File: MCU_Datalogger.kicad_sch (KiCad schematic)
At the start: 25 parts, among them U1 24LC1025, U2 DS1337S_, U3 24LC1025, U4 ATMEGA328P-AU, Y1 32.768 KHz, Y2 16 MHz

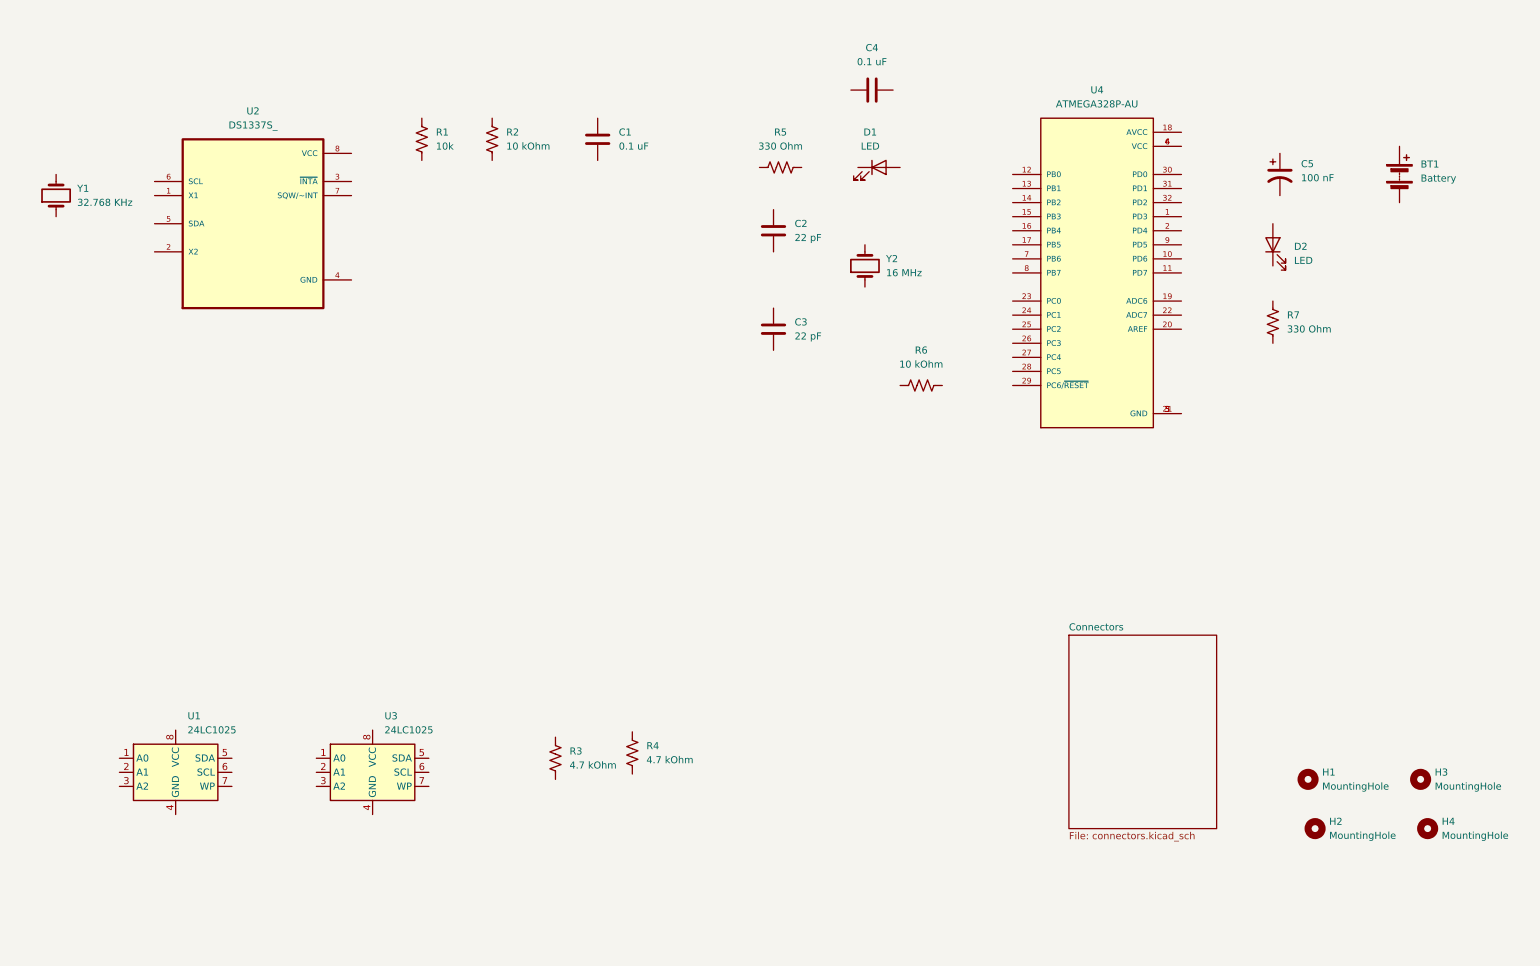
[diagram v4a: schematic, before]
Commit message: Wiring and adding netlabels to the schematic diagram for the main schematic page
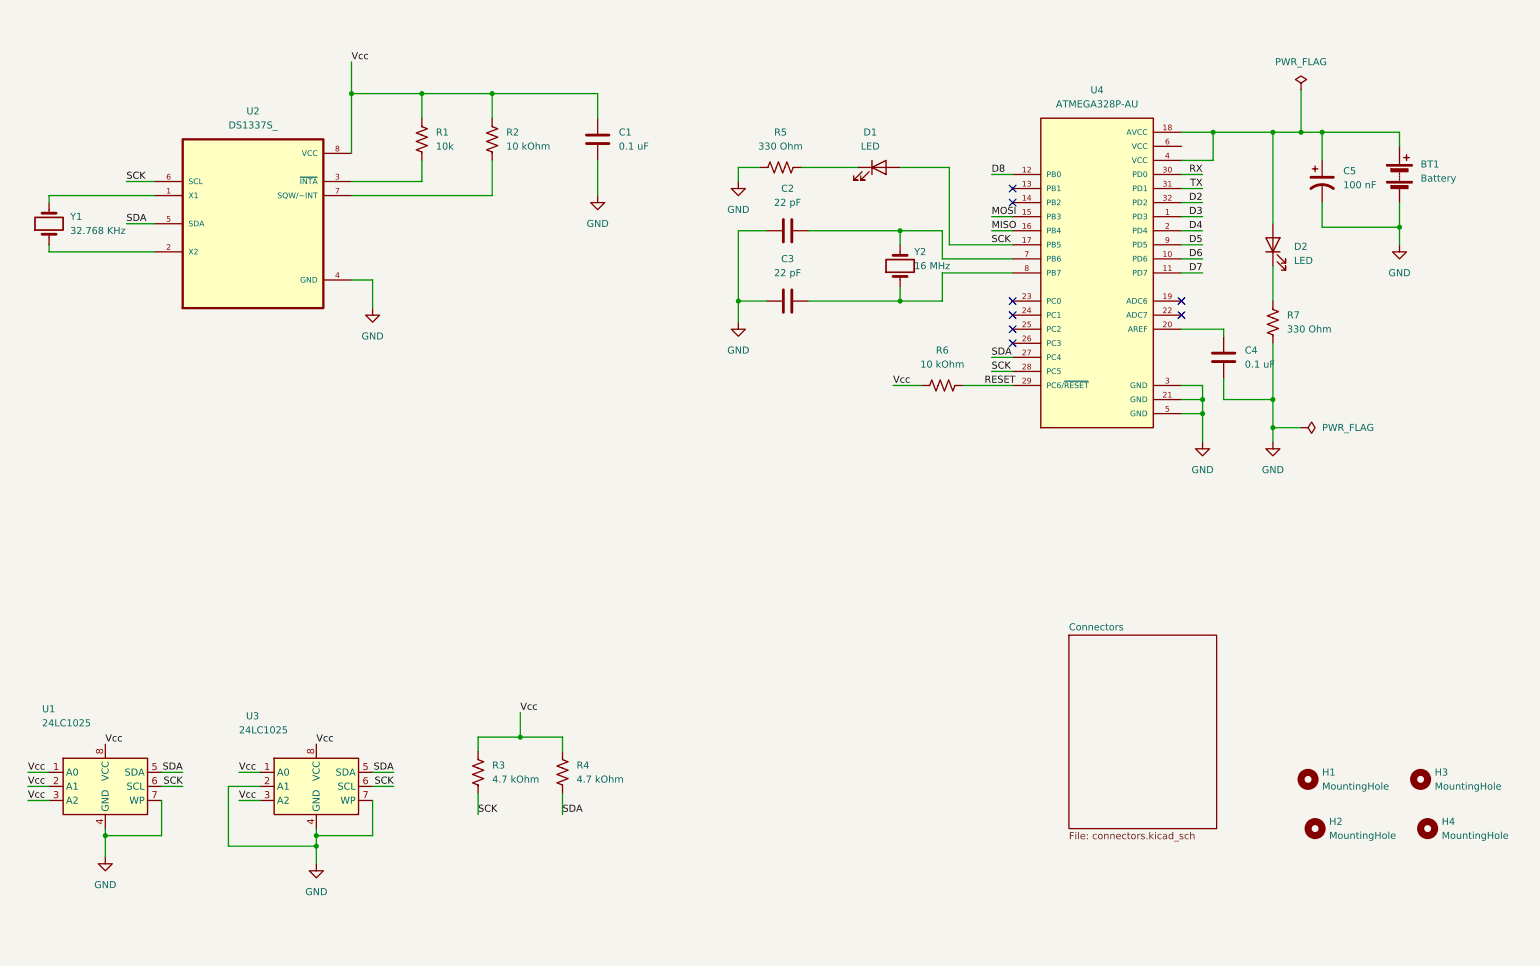
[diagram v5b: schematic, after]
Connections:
- net at U2.1 (X1): now also Y1.2
- net at U2.2 (X2): now also Y1.1
- net at U2.3 (~{INTA}): now also R1.2
- net GND: now reaches U2.4 (GND)
- net GND: now also BT1.2 (-), C1.2, C2.1, C3.1, C4.1, C5.2, R5.1, R7.2, U1.4 (GND), U1.7 (WP), U3.2 (A1), U3.4 (GND), U3.7 (WP), U4.21 (GND), U4.3 (GND), U4.5 (GND)
- net SDA: now reaches U2.5 (SDA)
- net SDA: now also R4.2, U1.5 (SDA), U3.5 (SDA), U4.27 (PC4)
- net SCK: now reaches U2.6 (SCL)
- net SCK: now also D1.2 (A), R3.2, U1.6 (SCL), U3.6 (SCL), U4.17 (PB5), U4.28 (PC5)
- net at U2.7 (SQW/~INT): now also R2.2
- net Vcc: now reaches U2.8 (VCC)
- net Vcc: now also C1.1, R1.1, R2.1, R3.1, R4.1, R6.1, U1.1 (A0), U1.2 (A1), U1.3 (A2), U1.8 (VCC), U3.1 (A0), U3.3 (A2), U3.8 (VCC)
- net at C2.2: now also U4.7 (PB6), Y2.2
- net at BT1.1 (+): now also C5.1, D2.2 (A), U4.18 (AVCC), U4.4 (VCC)
- net RESET: now reaches R6.2
- net RESET: now also U4.29 (PC6/~{RESET})
- net at D2.1 (K): now also R7.1
- net D3: now reaches U4.1 (PD3)
- net D6: now reaches U4.10 (PD6)
- net D7: now reaches U4.11 (PD7)
- net D8: now reaches U4.12 (PB0)
- net MOSI: now reaches U4.15 (PB3)
- net MISO: now reaches U4.16 (PB4)
- net D4: now reaches U4.2 (PD4)
- net at U4.20 (AREF): now also C4.2
- net RX: now reaches U4.30 (PD0)
- net TX: now reaches U4.31 (PD1)
- net D2: now reaches U4.32 (PD2)
- net at U4.6 (VCC): no longer U4.4 (VCC)
- net at U4.8 (PB7): now also C3.2, Y2.1
- net D5: now reaches U4.9 (PD5)
- net at D1.1 (K): now also R5.2
- no-connect marks 0 -> 8
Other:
- moved on the sheet: C2, C3, C4, C5, R3, R6, U1, U3, Y1, Y2

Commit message: Completed schematic wiring and passed ERC
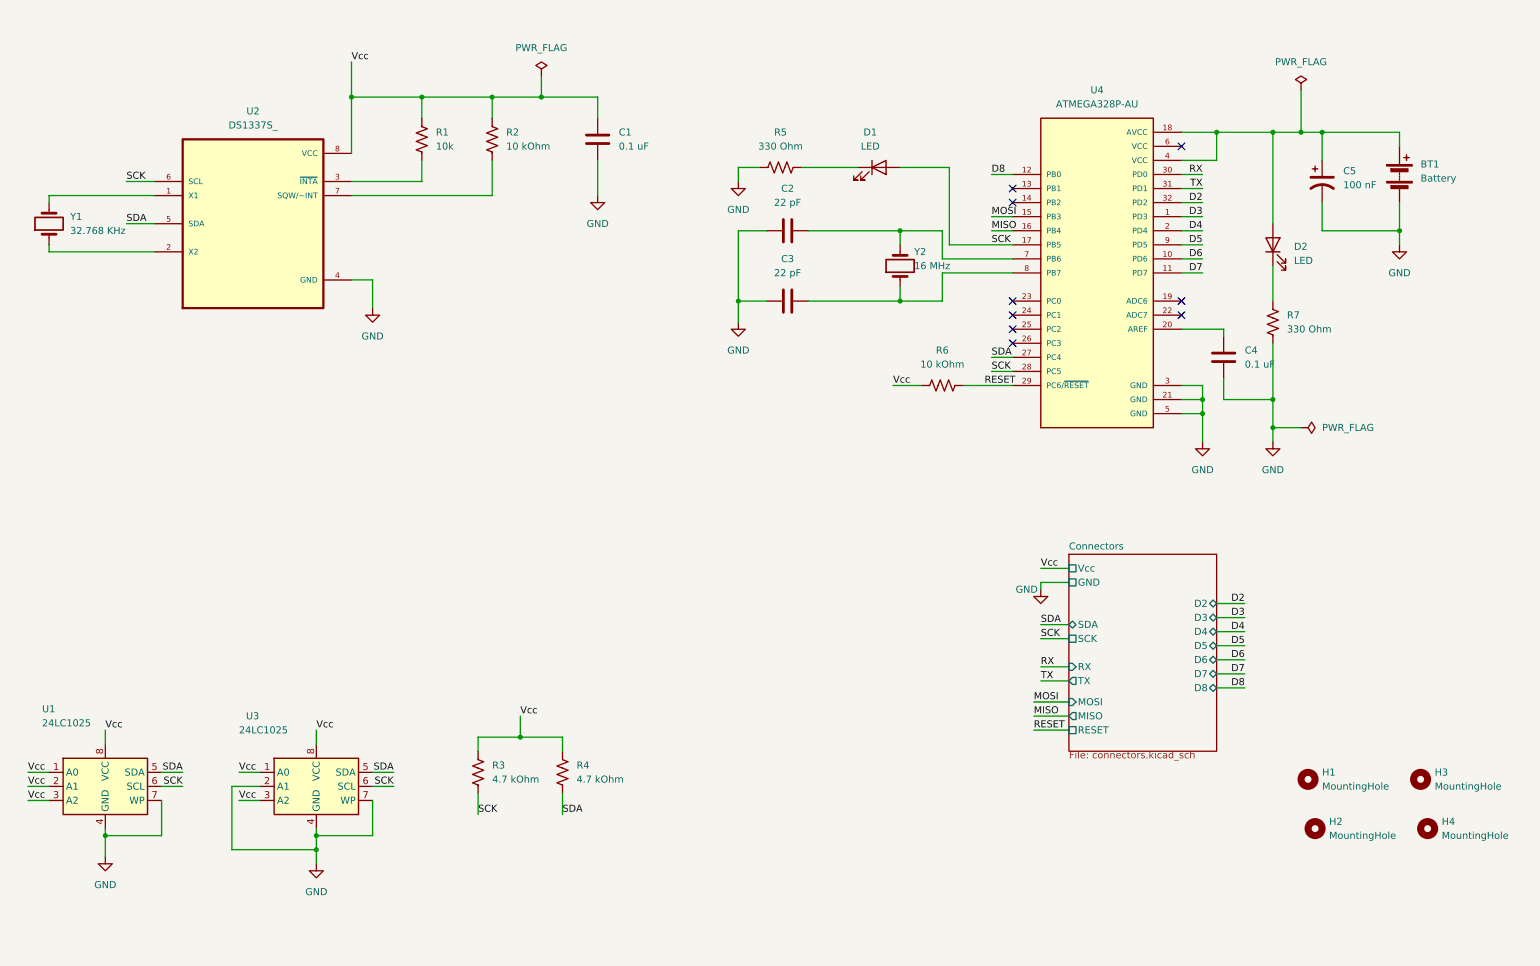
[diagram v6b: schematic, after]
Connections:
- no-connect marks 8 -> 9
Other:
- sheet Connectors ports: added D2, D3, D4, D5, D6, D7, D8, GND, MISO, MOSI, RESET, RX, SCK, SDA, TX, Vcc; removed none

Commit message: added comments to schematic
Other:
- note added: "MCU"
- note added: "Memory"
- note added: "Real time clock"
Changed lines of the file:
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@@
 		(comment 1 "Matt Cramer")
+	)
+	(text "Memory"
+		(exclude_from_sim no)
+		(at 19.05 125.73 0)
+		(effects
+			(font
+				(size 1.27 1.27)
+			)
+		)
+	)
+	(text "Real time clock"
+		(exclude_from_sim no)
+		(at 24.13 15.24 0)
+		(effects
+			(font
+				(size 1.27 1.27)
+			)
+		)
+	)
+	(text "MCU\n"
+		(exclude_from_sim no)
+		(at 144.78 17.78 0)
+		(effects
+			(font
+				(size 1.27 1.27)
+			)
+		)
 	)
 	(junction
@@
 		)
 	)
+	(polyline
+		(pts
+			(xy 142.875 19.05) (xy 273.05 19.05)
+		)
+		(stroke
+			(width 0)
+			(type default)
+		)
+	)
 	(wire
 		(pts
@@
 		)
 	)
+	(polyline
+		(pts
+			(xy 127 184.15) (xy 15.875 184.15)
+		)
+		(stroke
+			(width 0)
+			(type default)
+		)
+	)
 	(wire
 		(pts
@@
 		)
 	)
+	(polyline
+		(pts
+			(xy 136.525 76.2) (xy 136.525 15.875)
+		)
+		(stroke
+			(width 0)
+			(type default)
+		)
+	)
 	(wire
 		(pts
@@
 		)
 	)
+	(polyline
+		(pts
+			(xy 15.875 127) (xy 127 127)
+		)
+		(stroke
+			(width 0)
+			(type default)
+		)
+	)
 	(wire
 		(pts
@@
 		)
 	)
+	(polyline
+		(pts
+			(xy 15.875 76.2) (xy 136.525 76.2)
+		)
+		(stroke
+			(width 0)
+			(type default)
+		)
+	)
 	(wire
 		(pts
@@
 		)
 	)
+	(polyline
+		(pts
+			(xy 15.875 15.875) (xy 15.875 76.2)
+		)
+		(stroke
+			(width 0)
+			(type default)
+		)
+	)
 	(wire
 		(pts
@@
 		)
 	)
+	(polyline
+		(pts
+			(xy 273.05 19.05) (xy 273.05 98.425)
+		)
+		(stroke
+			(width 0)
+			(type default)
+		)
+	)
 	(wire
 		(pts
@@
 		)
 	)
+	(polyline
+		(pts
+			(xy 127 127) (xy 127 184.15)
+		)
+		(stroke
+			(width 0)
+			(type default)
+		)
+	)
 	(wire
 		(pts
@@
 		)
 	)
+	(polyline
+		(pts
+			(xy 15.875 127) (xy 15.875 184.15)
+		)
+		(stroke
+			(width 0)
+			(type default)
+		)
+	)
 	(wire
 		(pts
@@
 		)
 	)
+	(polyline
+		(pts
+			(xy 136.525 15.875) (xy 15.875 15.875)
+		)
+		(stroke
+			(width 0)
+			(type default)
+		)
+	)
 	(wire
 		(pts
@@
 		)
 	)
+	(polyline
+		(pts
+			(xy 273.05 98.425) (xy 142.875 98.425)
+		)
+		(stroke
+			(width 0)
+			(type default)
+		)
+	)
 	(wire
 		(pts
@@
 		)
 		(stroke
+			(width 0)
+			(type default)
+		)
+	)
+	(polyline
+		(pts
+			(xy 142.875 19.05) (xy 142.875 98.425)
+		)
+		(stroke

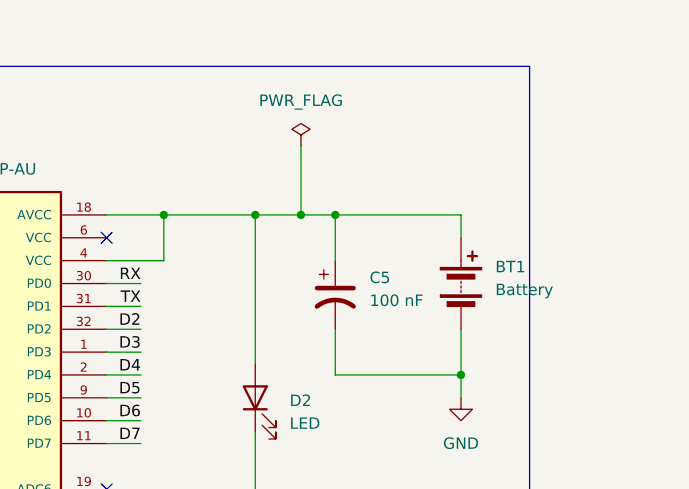
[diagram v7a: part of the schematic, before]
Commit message: fixed issue with VCC
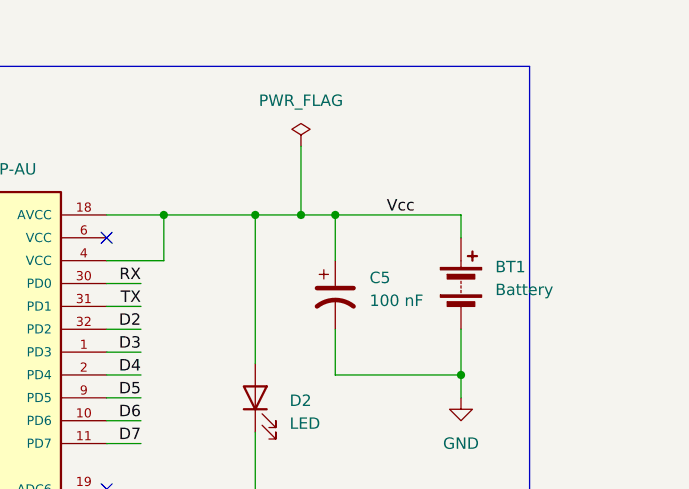
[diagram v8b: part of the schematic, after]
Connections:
- net Vcc: now also BT1.1 (+), C5.1, D2.2 (A), U4.18 (AVCC), U4.4 (VCC)
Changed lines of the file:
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@@
+		)
+	)
+	(label "Vcc"
+		(at 257.175 35.56 0)
+		(effects
+			(font
+				(size 1.27 1.27)
+			)
+			(justify left bottom)
 		)
 	)
